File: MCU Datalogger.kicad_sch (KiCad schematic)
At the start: 26 parts, among them U1 24LC1025, U2 24LC1025, U3 DS1337S_, U4 DS1337S_, U5 ATMEGA328P-AUR, Y1 Crystal, Y2 Crystal

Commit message: Added component values
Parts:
- C1, C2: value C -> 22pF
- C3, C4: value C -> 0.1uF
- C5: value C_Polarized -> 100nF
- R1, R6: value R -> 4.7K
- R2, R3, R5: value R -> 10K
- R4, R7: value R -> 330
- Y1: value Crystal -> 32.768 Khz
- Y2: value Crystal -> 16Mhz
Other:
- moved on the sheet: C2, R2
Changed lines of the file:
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@@
 			)
 		)
-		(property "Value" "C"
+		(property "Value" "0.1uF"
 			(at 159.499 24.0495 90)
 			(effects
@@
 			)
 		)
+		(property "Purpose" ""
+			(at 159.499 28.6267 0)
+			(effects
+				(font
+					(size 1.27 1.27)
+				)
+			)
+		)
 		(pin "1"
 		)
@@
 			)
 		)
-		(property "Value" "C_Polarized"
+		(property "Value" "100nF"
 			(at 268.0699 46.849 0)
 			(effects
@@
 			)
 		)
+		(property "Purpose" ""
+			(at 265.0615 46.4681 0)
+			(effects
+				(font
+					(size 1.27 1.27)
+				)
+			)
+		)
 		(pin "2"
 		)
@@
 			)
 		)
-		(property "Value" "R"
+		(property "Value" "330"
 			(at 147.0099 44.3695 90)
 			(effects
@@
 			)
 		)
+		(property "Purpose" ""
+			(at 147.0099 47.3603 0)
+			(effects
+				(font
+					(size 1.27 1.27)
+				)
+			)
+		)
 		(pin "2"
 		)
@@
 			)
 		)
-		(property "Value" "C"
+		(property "Value" "0.1uF"
 			(at 135.8663 49.4665 0)
 			(effects
@@
 			)
 		)
+		(property "Purpose" ""
+			(at 131.8446 48.1966 0)
+			(effects
+				(font
+					(size 1.27 1.27)
+				)
+			)
+		)
 		(pin "2"
 		)
@@
 	(symbol
 		(lib_id "Device:C")
-		(at 146.7125 62.2282 0)
+		(at 145.8023 63.2336 0)
 		(unit 1)
 		(exclude_from_sim no)
@@
 		(dnp no)
 		(property "Reference" "C2"
-			(at 150.9541 61.0944 0)
-			(effects
-				(font
-					(size 1.27 1.27)
-				)
-				(justify left)
-			)
-		)
-		(property "Value" "C"
-			(at 150.9541 63.6344 0)
-			(effects
-				(font
-					(size 1.27 1.27)
-				)
-				(justify left)
-			)
-		)
-		(property "Footprint" ""
-			(at 147.6777 66.0382 0)
-			(effects
-				(font
-					(size 1.27 1.27)
-				)
-				(hide yes)
-			)
-		)
-		(property "Datasheet" "~"
-			(at 146.7125 62.2282 0)
+			(at 150.0439 62.0998 0)
+			(effects
+				(font
+					(size 1.27 1.27)
+				)
+				(justify left)
+			)
+		)
+		(property "Value" "22pF"
+			(at 150.0439 64.6398 0)
+			(effects
+				(font
+					(size 1.27 1.27)
+				)
+				(justify left)
+			)
+		)
+		(property "Footprint" ""
+			(at 146.7675 67.0436 0)
+			(effects
+				(font
+					(size 1.27 1.27)
+				)
+				(hide yes)
+			)
+		)
+		(property "Datasheet" "~"
+			(at 145.8023 63.2336 0)
 			(effects
 				(font
@@
 		)
 		(property "Description" "Unpolarized capacitor"
-			(at 146.7125 62.2282 0)
-			(effects
-				(font
-					(size 1.27 1.27)
-				)
-				(hide yes)
+			(at 145.8023 63.2336 0)
+			(effects
+				(font
+					(size 1.27 1.27)
+				)
+				(hide yes)
+			)
+		)
+		(property "Purpose" ""
+			(at 145.8023 63.2336 0)
+			(effects
+				(font
+					(size 1.27 1.27)
+				)
 			)
 		)
@@
 			)
 		)
-		(property "Value" "R"
+		(property "Value" "330"
 			(at 270.3697 74.7977 0)
 			(effects
@@
 			)
 		)
+		(property "Purpose" ""
+			(at 267.4403 73.5278 0)
+			(effects
+				(font
+					(size 1.27 1.27)
+				)
+			)
+		)
 		(pin "2"
 		)
@@
 			)
 		)
-		(property "Value" "R"
+		(property "Value" "4.7K"
 			(at 109.4175 147.9606 0)
 			(effects
@@
 			)
 		)
+		(property "Purpose" ""
+			(at 107.5537 146.6907 0)
+			(effects
+				(font
+					(size 1.27 1.27)
+				)
+			)
+		)
 		(pin "2"
 		)
@@
 			)
 		)
-		(property "Value" "R"
+		(property "Value" "4.7K"
 			(at 117.0375 148.0037 0)
 			(effects
@@
 			)
 		)
+		(property "Purpose" ""
+			(at 114.8951 146.7338 0)
+			(effects
+				(font
+					(size 1.27 1.27)
+				)
+			)
+		)
 		(pin "1"
 		)
@@
 			)
 		)
-		(property "Value" "Crystal"
+		(property "Value" "16Mhz"
 			(at 163.5019 64.3902 90)
 			(effects
@@
 			)
 		)
+		(property "Purpose" ""
+			(at 159.5547 63.1203 0)
+			(effects
+				(font
+					(size 1.27 1.27)
+				)
+			)
+		)
 		(pin "2"
 		)
@@
 			)
 		)
-		(property "Value" "C"
+		(property "Value" "22pF"
 			(at 150.26 76.2846 0)
 			(effects
@@
 			)
 		)
+		(property "Purpose" ""
+			(at 147.3073 75.0147 0)
+			(effects
+				(font
+					(size 1.27 1.27)
+				)
+			)
+		)
 		(pin "2"
 		)
@@
 			)
 		)
-		(property "Value" "Crystal"
+		(property "Value" "32.768 Khz"
 			(at 24.13 70.6347 90)
 			(effects
@@
 			)
 		)
+		(property "Purpose" ""
+			(at 20.2792 69.3648 0)
+			(effects
+				(font
+					(size 1.27 1.27)
+				)
+			)
+		)
 		(pin "1"
 		)
@@
 			)
 		)
-		(property "Value" "R"
+		(property "Value" "10K"
 			(at 122.7077 50.1169 0)
 			(effects
@@
 			)
 		)
+		(property "Purpose" ""
+			(at 120.2476 48.847 0)
+			(effects
+				(font
+					(size 1.27 1.27)
+				)
+			)
+		)
 		(pin "2"
 		)
@@
 			)
 		)
-		(property "Value" "R"
+		(property "Value" "10K"
 			(at 160.6884 74.8495 90)
 			(effects
@@
 			)
 		)
+		(property "Purpose" ""
+			(at 160.6884 77.9883 0)
+			(effects
+				(font
+					(size 1.27 1.27)
+				)
+			)
+		)
 		(pin "1"
 		)
@@
 	(symbol
 		(lib_id "Device:R")
-		(at 113.4648 48.0331 0)
+		(at 113.057 49.0234 0)
 		(unit 1)
 		(exclude_from_sim no)
@@
 		(fields_autoplaced yes)
 		(property "Reference" "R2"
-			(at 116.173 46.763 0)
-			(effects
-				(font
-					(size 1.27 1.27)
-				)
-				(justify left)
-			)
-		)
-		(property "Value" "R"
-			(at 116.173 49.303 0)
-			(effects
-				(font
-					(size 1.27 1.27)
-				)
-				(justify left)
-			)
-		)
-		(property "Footprint" ""
-			(at 111.6868 48.0331 90)
-			(effects
-				(font
-					(size 1.27 1.27)
-				)
-				(hide yes)
-			)
-		)
-		(property "Datasheet" "~"
-			(at 113.4648 48.0331 0)
+			(at 115.7652 47.7533 0)
+			(effects
+				(font
+					(size 1.27 1.27)
+				)
+				(justify left)
+			)
+		)
+		(property "Value" "10K"
+			(at 115.7652 50.2933 0)
+			(effects
+				(font
+					(size 1.27 1.27)
+				)
+				(justify left)
+			)
+		)
+		(property "Footprint" ""
+			(at 111.279 49.0234 90)
+			(effects
+				(font
+					(size 1.27 1.27)
+				)
+				(hide yes)
+			)
+		)
+		(property "Datasheet" "~"
+			(at 113.057 49.0234 0)
 			(effects
 				(font
@@
 		)
 		(property "Description" "Resistor"
-			(at 113.4648 48.0331 0)
-			(effects
-				(font
-					(size 1.27 1.27)
-				)
-				(hide yes)
-			)
-		)
+			(at 113.057 49.0234 0)
+			(effects
+				(font
+					(size 1.27 1.27)
+				)
+				(hide yes)
+			)
+		)
+		(property "Purpose" ""
+			(at 113.057 49.0234 0)
+			(effects
+				(font
+					(size 1.27 1.27)
+				)
+			)
+		)

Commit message: Footprint associations
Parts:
- removed U4: DS1337S_, DS1337S_:SOIC127P600X175-8N, symbol DS1337S_:DS1337S_
- C1, C2, C3, C4, C5: footprint (none) -> Capacitor_SMD:C_0805_2012Metric
- D1, D2: footprint (none) -> LED_SMD:LED_0805_2012Metric
- R1, R2, R3, R4, R5, R6, R7: footprint (none) -> Resistor_SMD:R_0805_2012Metric
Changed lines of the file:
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@@
 			)
 		)
-		(property "Footprint" ""
+		(property "Footprint" "Capacitor_SMD:C_0805_2012Metric"
 			(at 155.689 29.5919 0)
 			(effects
@@
 			)
 		)
-		(property "Footprint" ""
+		(property "Footprint" "Capacitor_SMD:C_0805_2012Metric"
 			(at 266.0267 50.2781 0)
 			(effects
@@
 			)
 		)
-		(property "Footprint" ""
+		(property "Footprint" "Resistor_SMD:R_0805_2012Metric"
 			(at 147.0099 49.1383 90)
 			(effects
@@
 			)
 		)
-		(property "Footprint" ""
+		(property "Footprint" "Capacitor_SMD:C_0805_2012Metric"
 			(at 132.8098 52.0066 0)
 			(effects
@@
 			)
 		)
-		(property "Footprint" ""
+		(property "Footprint" "Capacitor_SMD:C_0805_2012Metric"
 			(at 146.7675 67.0436 0)
 			(effects
@@
 	)
 	(symbol
-		(lib_id "DS1337S_:DS1337S_")
-		(at 85.7539 56.281 0)
-		(unit 1)
-		(exclude_from_sim no)
-		(in_bom yes)
-		(on_board yes)
-		(dnp no)
-		(fields_autoplaced yes)
-		(property "Reference" "U4"
-			(at 85.7539 35.8014 0)
-			(effects
-				(font
-					(size 1.27 1.27)
-				)
-			)
-		)
-		(property "Value" "DS1337S_"
-			(at 85.7539 38.3414 0)
-			(effects
-				(font
-					(size 1.27 1.27)
-				)
-			)
-		)
-		(property "Footprint" "DS1337S_:SOIC127P600X175-8N"
-			(at 85.7539 56.281 0)
-			(effects
-				(font
-					(size 1.27 1.27)
-				)
-				(justify bottom)
-				(hide yes)
-			)
-		)
-		(property "Datasheet" ""
-			(at 85.7539 56.281 0)
-			(effects
-				(font
-					(size 1.27 1.27)
-				)
-				(hide yes)
-			)
-		)
-		(property "Description" ""
-			(at 85.7539 56.281 0)
-			(effects
-				(font
-					(size 1.27 1.27)
-				)
-				(hide yes)
-			)
-		)
-		(property "MF" "Analog Devices"
-			(at 85.7539 56.281 0)
-			(effects
-				(font
-					(size 1.27 1.27)
-				)
-				(justify bottom)
-				(hide yes)
-			)
-		)
-		(property "Description_1" "I²C Serial Real-Time Clock"
-			(at 85.7539 56.281 0)
-			(effects
-				(font
-					(size 1.27 1.27)
-				)
-				(justify bottom)
-				(hide yes)
-			)
-		)
-		(property "Package" "SOIC-8 Maxim"
-			(at 85.7539 56.281 0)
-			(effects
-				(font
-					(size 1.27 1.27)
-				)
-				(justify bottom)
-				(hide yes)
-			)
-		)
-		(property "Price" "None"
-			(at 85.7539 56.281 0)
-			(effects
-				(font
-					(size 1.27 1.27)
-				)
-				(justify bottom)
-				(hide yes)
-			)
-		)
-		(property "SnapEDA_Link" "https://www.snapeda.com/parts/DS1337S+/Analog+Devices/view-part/?ref=snap"
-			(at 85.7539 56.281 0)
-			(effects
-				(font
-					(size 1.27 1.27)
-				)
-				(justify bottom)
-				(hide yes)
-			)
-		)
-		(property "MP" "DS1337S+"
-			(at 85.7539 56.281 0)
-			(effects
-				(font
-					(size 1.27 1.27)
-				)
-				(justify bottom)
-				(hide yes)
-			)
-		)
-		(property "Purchase-URL" "https://www.snapeda.com/api/url_track_click_mouser/?unipart_id=105732&manufacturer=Analog Devices&part_name=DS1337S+&search_term=ds1337s"
-			(at 85.7539 56.281 0)
-			(effects
-				(font
-					(size 1.27 1.27)
-				)
-				(justify bottom)
-				(hide yes)
-			)
-		)
-		(property "Availability" "In Stock"
-			(at 85.7539 56.281 0)
-			(effects
-				(font
-					(size 1.27 1.27)
-				)
-				(justify bottom)
-				(hide yes)
-			)
-		)
-		(property "Check_prices" "https://www.snapeda.com/parts/DS1337S+/Analog+Devices/view-part/?ref=eda"
-			(at 85.7539 56.281 0)
-			(effects
-				(font
-					(size 1.27 1.27)
-				)
-				(justify bottom)
-				(hide yes)
-			)
-		)
-		(pin "1"
-		)
-		(pin "5"
-		)
-		(pin "2"
-		)
-		(pin "3"
-		)
-		(pin "8"
-		)
-		(pin "6"
-		)
-		(pin "7"
-		)
-		(pin "4"
-		)
-		(instances
-			(project ""
-				(path "/e37b0ca1-9fe1-4575-b9a4-8036a316ab3d"
-					(reference "U4")
-					(unit 1)
-				)
-			)
-		)
-	)
-	(symbol
 		(lib_id "Device:R")
 		(at 267.4403 73.5278 0)
@@
 			)
 		)
-		(property "Footprint" ""
+		(property "Footprint" "Resistor_SMD:R_0805_2012Metric"
 			(at 265.6623 73.5278 90)
 			(effects
@@
 			)
 		)
-		(property "Footprint" ""
+		(property "Footprint" "Resistor_SMD:R_0805_2012Metric"
 			(at 105.7757 146.6907 90)
 			(effects
@@
 			)
 		)
-		(property "Footprint" ""
+		(property "Footprint" "Resistor_SMD:R_0805_2012Metric"
 			(at 113.1171 146.7338 90)
 			(effects
@@
 			)
 		)
-		(property "Footprint" ""
+		(property "Footprint" "LED_SMD:LED_0805_2012Metric"
 			(at 267.1986 60.1467 0)
 			(effects
@@
 			)
 		)
-		(property "Footprint" ""
+		(property "Footprint" "Capacitor_SMD:C_0805_2012Metric"
 			(at 148.2725 78.8247 0)
 			(effects
@@
 			)
 		)
-		(property "Footprint" ""
+		(property "Footprint" "Resistor_SMD:R_0805_2012Metric"
 			(at 118.4696 48.847 90)
 			(effects
@@
 			)
 		)
-		(property "Footprint" ""
+		(property "Footprint" "Resistor_SMD:R_0805_2012Metric"
 			(at 160.6884 79.7663 90)
 			(effects
@@
 			)
 		)
-		(property "Footprint" ""
+		(property "Footprint" "LED_SMD:LED_0805_2012Metric"
 			(at 161.3388 41.7105 0)
 			(effects
@@
 			)
 		)
-		(property "Footprint" ""
+		(property "Footprint" "Resistor_SMD:R_0805_2012Metric"
 			(at 111.279 49.0234 90)
 			(effects

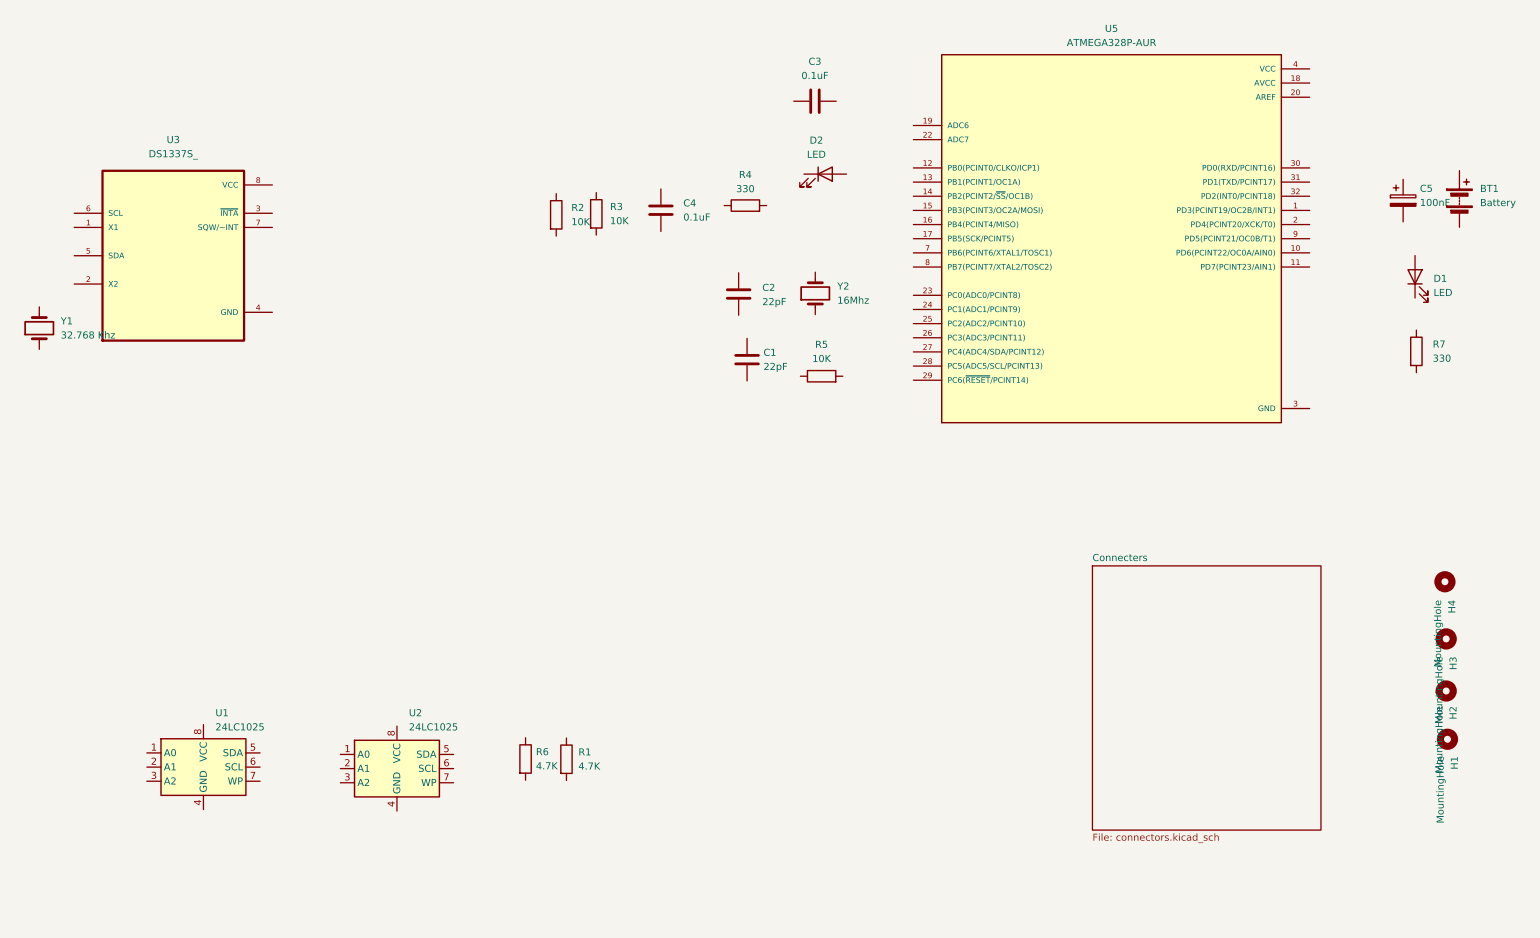
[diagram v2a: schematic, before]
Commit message: Wires are connected in Schema 1
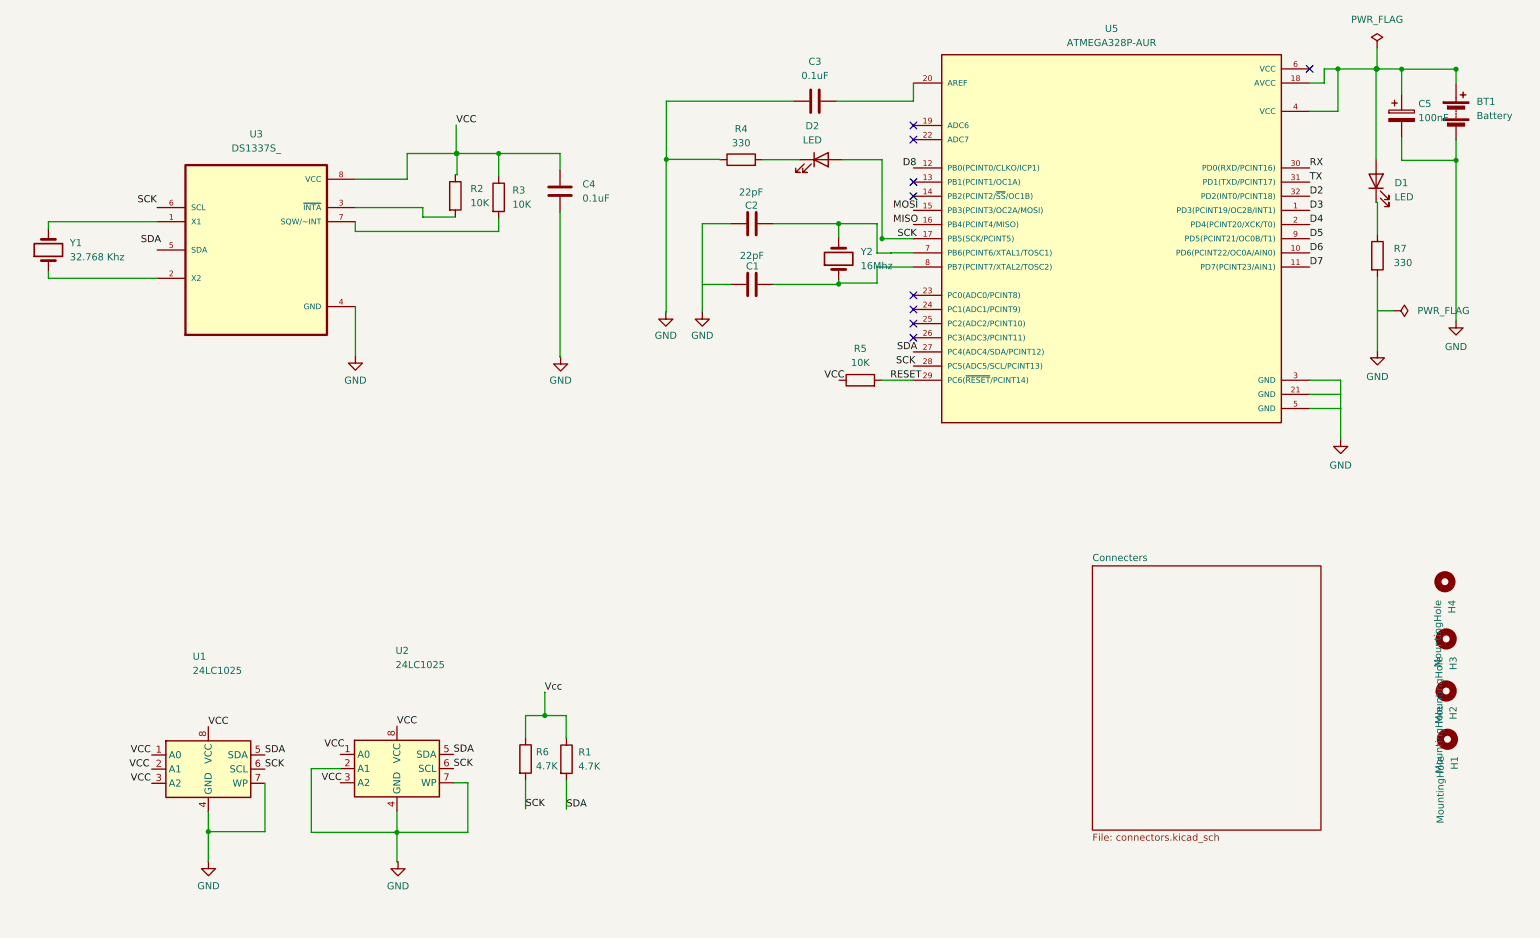
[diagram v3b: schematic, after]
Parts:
- BT1: footprint (none) -> Connector_PinHeader_2.54mm:PinHeader_1x02_P2.54mm_Vertical
- H1, H2, H3, H4: footprint (none) -> MountingHole:MountingHole_2.1mm
- U1, U2: footprint (none) -> Package_SO:SOIC-8_5.3x5.3mm_P1.27mm
- U3: footprint DS1337S_:SOIC127P600X175-8N -> Footprints:SOIC127P600X175-8N
- U5: footprint ATMEGA328P-AUR:QFP80P900X900X120-32N -> Footprints:QFP80P900X900X120-32N
- Y1, Y2: footprint (none) -> Crystal:Crystal_SMD_5032-2Pin_5.0x3.2mm_HandSoldering
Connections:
- net GND: now also BT1.2 (-), C2.1, C3.2, C4.2, C5.2, R4.1, R7.2, U1.4 (GND), U1.7 (WP), U2.2 (A1), U2.4 (GND), U2.7 (WP), U3.4 (GND); no longer U5.21 (GND), U5.5 (GND)
- net VCC: now also C4.1, R2.1, R3.1, U1.8 (VCC), U2.8 (VCC), U3.8 (VCC); no longer U5.4 (VCC), U5.6 (VCC)
- net at C3.1: now also U5.20 (AREF)
- net at C5.1: now also BT1.1 (+), D1.2 (A), U5.18 (AVCC), U5.4 (VCC)
- net at R4.2: now also D2.1 (K)
- net at C2.2: now also U5.7 (PB6(PCINT6/XTAL1/TOSC1)), Y2.2
- net at R7.1: now also D1.1 (K)
- net SDA: now reaches U2.5 (SDA)
- net SDA: now also R1.2, U1.5 (SDA)
- net SCK: now reaches U2.6 (SCL)
- net SCK: now also D2.2 (A), R6.2, U1.6 (SCL), U5.17 (PB5(SCK/PCINT5))
- net Vcc: now reaches R6.1
- net Vcc: now also R1.1
- net at Y2.1: now also C1.1, U5.8 (PB7(PCINT7/XTAL2/TOSC2))
- net at Y1.1: now also U3.2 (X2)
- net at Y1.2: now also U3.1 (X1)
- net at R3.2: now also U3.7 (SQW/~INT)
- net RESET: now reaches R5.2
- net RESET: now also U5.29 (PC6(~{RESET}/PCINT14))
- net at U3.3 (~{INTA}): now also R2.2
- net D3: now reaches U5.1 (PD3(PCINT19/OC2B/INT1))
- net D6: now reaches U5.10 (PD6(PCINT22/OC0A/AIN0))
- net D7: now reaches U5.11 (PD7(PCINT23/AIN1))
- net D4: now reaches U5.2 (PD4(PCINT20/XCK/T0))
- net RX: now reaches U5.30 (PD0(RXD/PCINT16))
- net TX: now reaches U5.31 (PD1(TXD/PCINT17))
- net D2: now reaches U5.32 (PD2(INT0/PCINT18))
- net D5: now reaches U5.9 (PD5(PCINT21/OC0B/T1))
- no-connect marks 0 -> 9
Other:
- moved on the sheet: BT1, C1, C2, C4, C5, D1, D2, R2, R3, R4, R5, R7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

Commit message: Completed wiring with electrical checker
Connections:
- net VCC is gone; now on net Vcc: C4.1, R2.1, R3.1, U1.8 (VCC), U2.8 (VCC), U3.8 (VCC)
- net D8: now also U5.12 (PB0(PCINT0/CLKO/ICP1))
- net GND: now also C1.2, U5.21 (GND), U5.5 (GND)
- net MISO: now also U5.16 (PB4(PCINT4/MISO))
- net MOSI: now also U5.15 (PB3(PCINT3/OC2A/MOSI))
- net SCK: no longer R6.2, U1.6 (SCL), U2.6 (SCL)
- net SDA: now also U3.5 (SDA), U5.27 (PC4(ADC4/SDA/PCINT12))
- net Vcc: now also BT1.1 (+), C5.1, D1.2 (A), R5.1, U1.1 (A0), U1.2 (A1), U1.3 (A2), U2.1 (A0), U2.3 (A2), U5.18 (AVCC), U5.4 (VCC), U5.6 (VCC)
- net SCL: now reaches U3.6 (SCL)
- net SCL: now also R6.2, U1.6 (SCL), U2.6 (SCL), U5.28 (PC5(ADC5/SCL/PCINT13))
- no-connect marks 9 -> 8
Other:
- sheet Connecters ports: added D2, D3, D4, D5, D6, D7, D8, GND, MISO, MOSI, RESET, RX, SCK, SCL, SDA, TX, Vcc; removed none
- moved on the sheet: C1, C3, C4, C5, D2, H3, H4, R1, R6, U2, U3, U5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

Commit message: Comments
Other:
- note added: "EEPROM"
- note added: "MCU"
- note added: "Mounting Holes"
- note added: "Real Time Clock"
